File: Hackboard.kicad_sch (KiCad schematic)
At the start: 61 parts, among them J1 Conn_01x31_Socket, J2 Micro_SD_Card, J3 Conn_01x31_Socket, J5 Barrel_Jack, J6 USB_C_Receptacle_USB2.0_16P, J7 Conn_02x02_Counter_Clockwise, Q1 NMOS, Q2 NMOS, Q3 NMOS, SW1 SW_MEC_5E, U1 NCP164CSN330T1G, U2 AP63205WU, U3 STM32L476RGT6, U7 USBLC6-2SC6

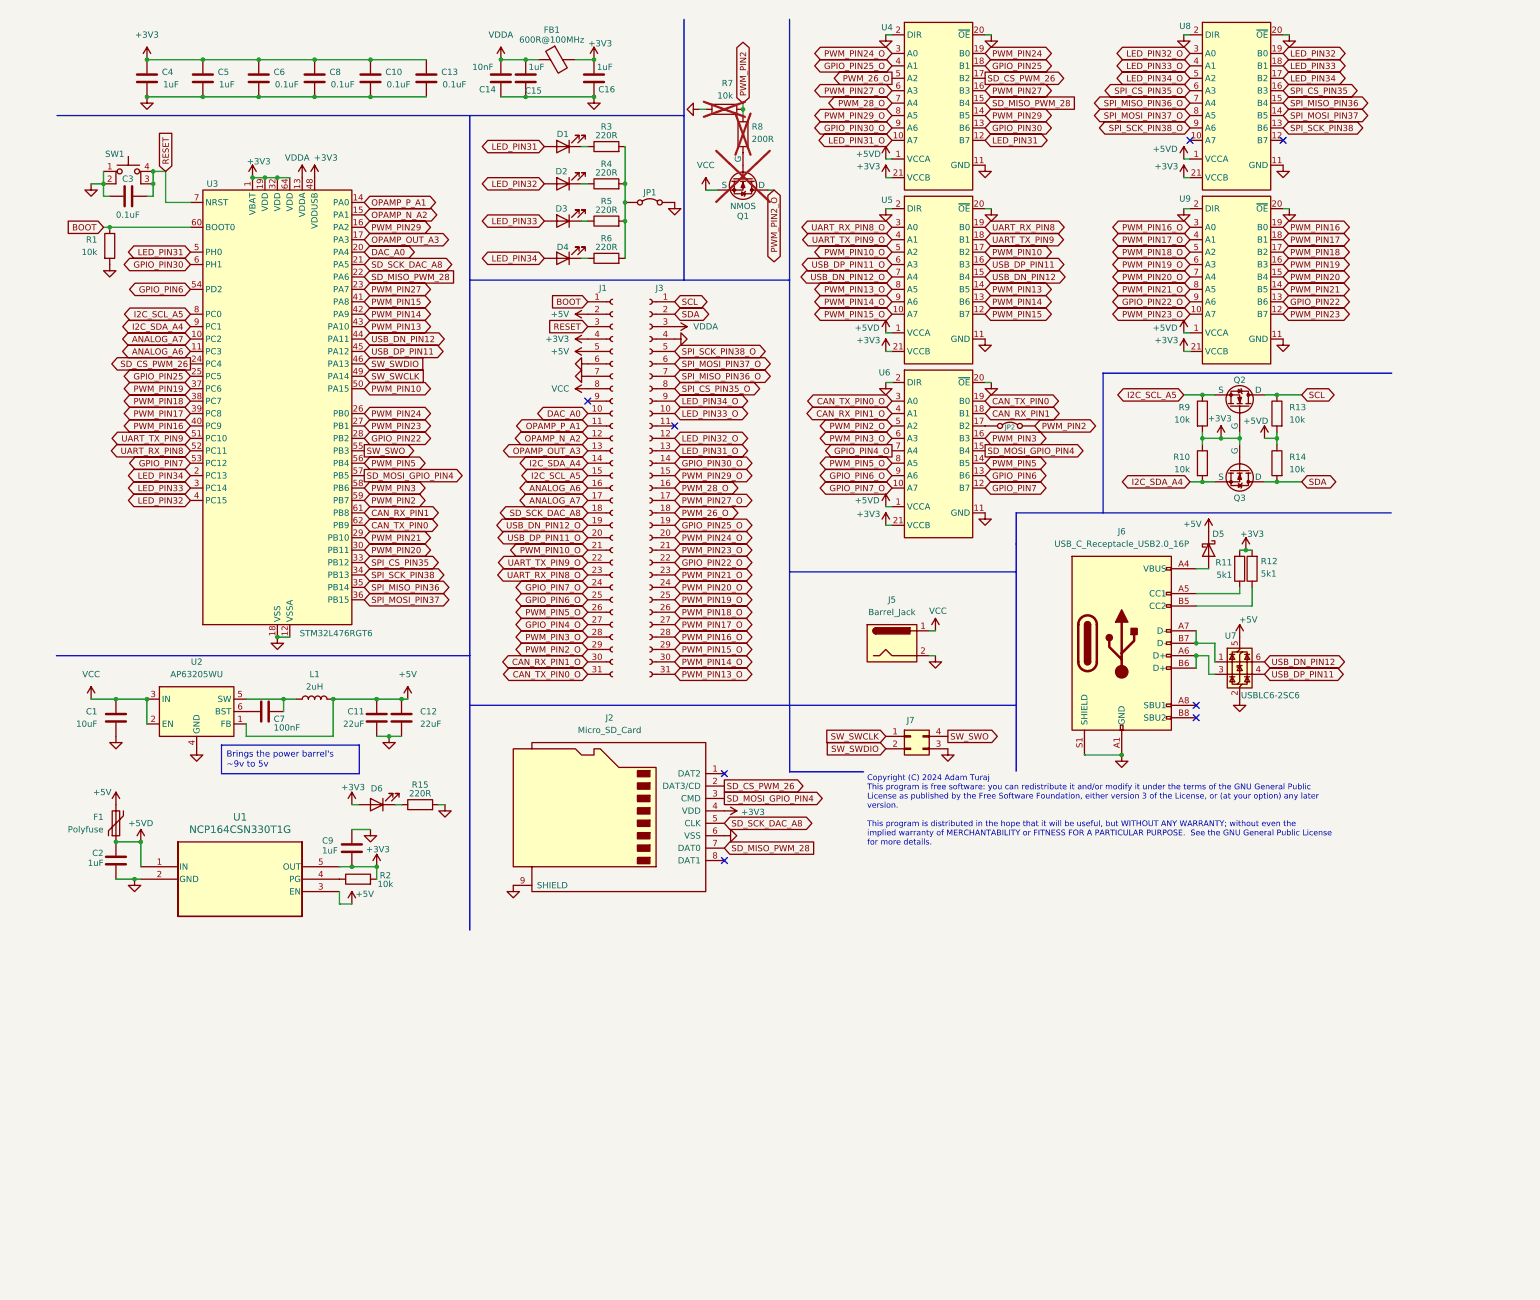
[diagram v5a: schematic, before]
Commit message: Finish footprints and place initial footprints on PCB editor
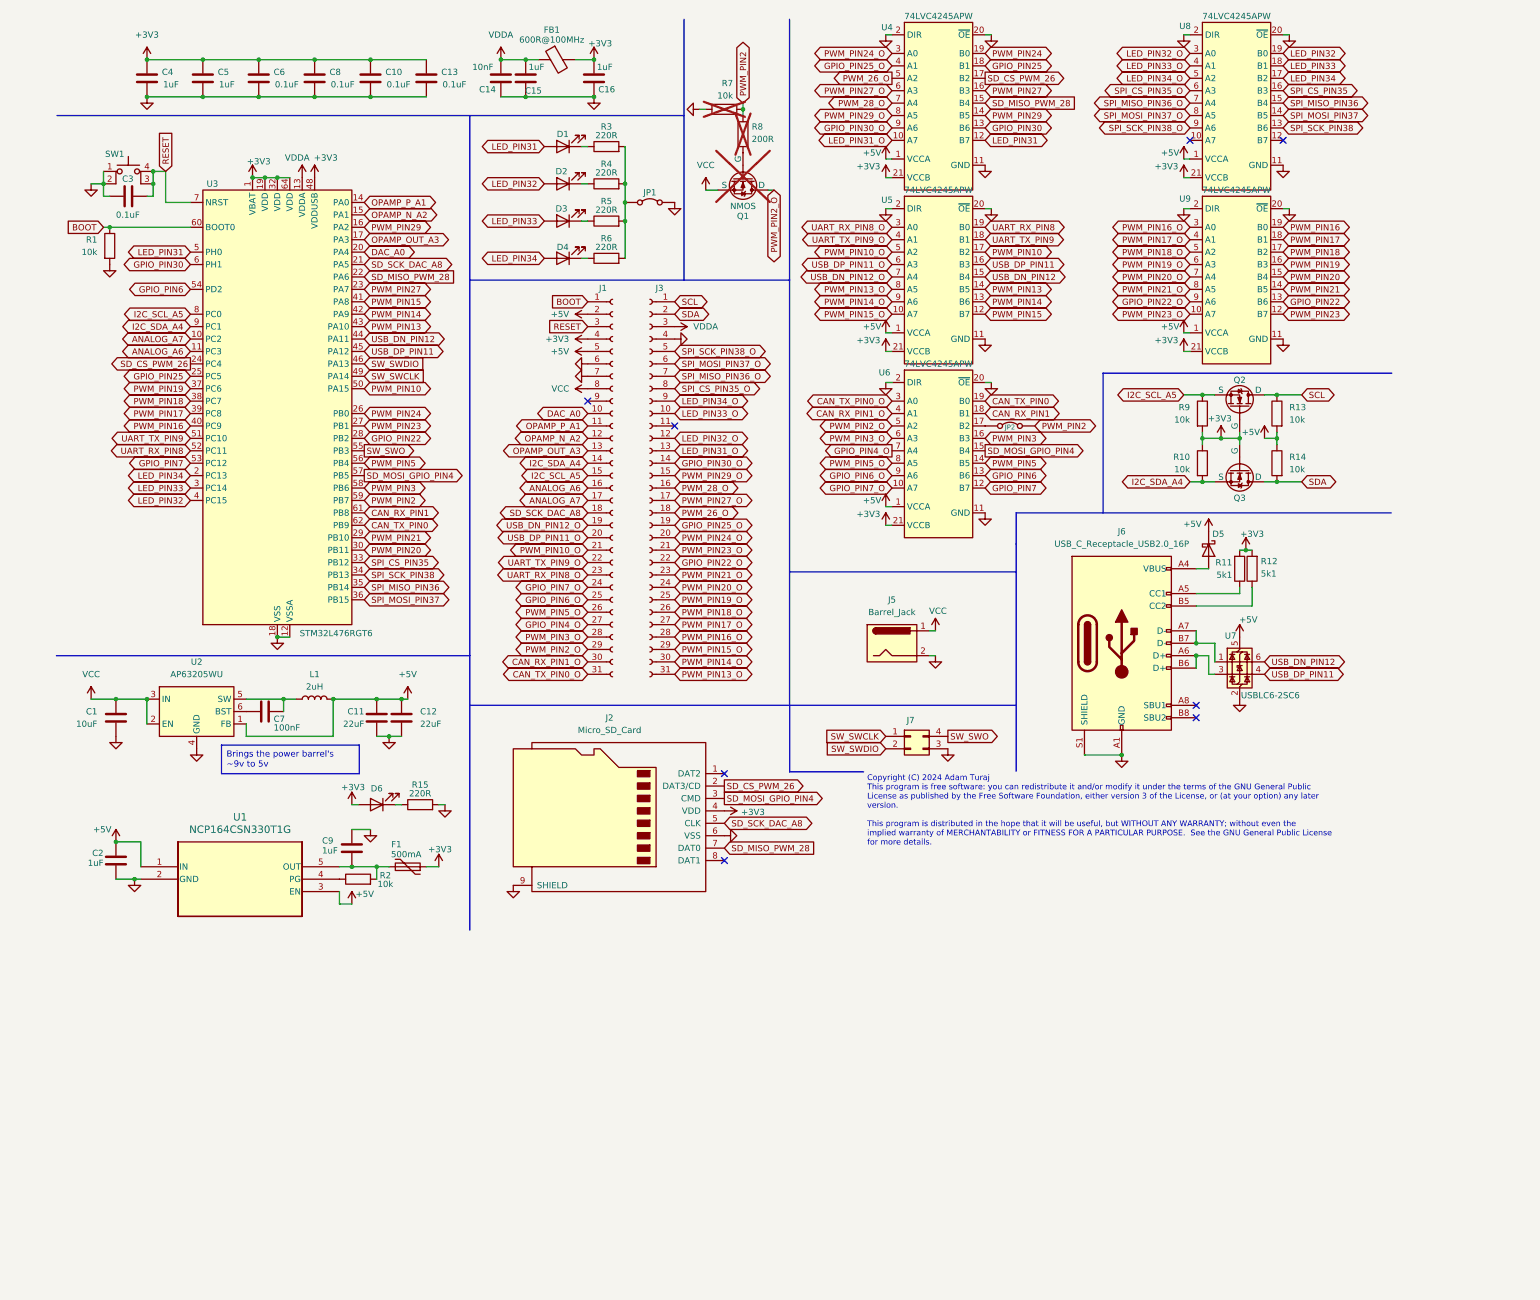
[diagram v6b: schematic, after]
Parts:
- F1: value Polyfuse -> 500mA; footprint (none) -> Fuse:Fuse_1812_4532Metric
- FB1: footprint (none) -> Inductor_SMD:L_0603_1608Metric
- J1, J3: footprint (none) -> Connector_PinHeader_2.54mm:PinHeader_1x31_P2.54mm_Vertical
- J2: footprint (none) -> Connector_Card:CONN9_MSD-1_CUD
- J5: footprint (none) -> Connector_BarrelJack:CUI_PJ-002AH
- J6: footprint (none) -> Connector_USB:USB_C_Receptacle_GCT_USB4105-xx-A_16P_TopMnt_Horizontal
- J7: footprint (none) -> Connector_PinHeader_2.54mm:PinHeader_2x02_P2.54mm_Vertical
- JP1, JP2: footprint (none) -> Jumper:SolderJumper-2_P1.3mm_Open_RoundedPad1.0x1.5mm
- Q1, Q2, Q3: footprint (none) -> Package_TO_SOT_SMD:SOT-23
- SW1: footprint (none) -> Button_Switch_SMD:SW_SPST_PTS645
- U1: footprint FP-NCP164CSN330T1G_OSI -> Package_SO:TSOP-5_1.65x3.05mm_P0.95mm
- U4, U5, U6, U8, U9: value ~ -> 74LVC4245APW; footprint (none) -> Package_SO:TSSOP-24_4.4x7.8mm_P0.65mm
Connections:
- net +3V3: now also F1.1; no longer C9.2, R2.2, U1.5 (OUT)
- net +5V: now also C2.1, R13.2, R14.1, U1.1 (IN), U4.1 (VCCA), U5.1 (VCCA), U6.1 (VCCA), U8.1 (VCCA), U9.1 (VCCA); no longer F1.2
- removed net +5VD: C2.1, F1.1, R13.2, R14.1, U1.1 (IN), U4.1 (VCCA), U5.1 (VCCA), U6.1 (VCCA), U8.1 (VCCA), U9.1 (VCCA)
- new net: C9.2, F1.2, R2.2, U1.5 (OUT)

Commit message: Make basis of out line and start placing components
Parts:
- removed J5: Barrel_Jack, Connector_BarrelJack:CUI_PJ-002AH, symbol Connector:Barrel_Jack
- removed SW1: SW_MEC_5E, Button_Switch_SMD:SW_SPST_PTS645, symbol Switch:SW_MEC_5E
- added A1: Arduino_UNO_R3, Module:Arduino_UNO_R3, symbol MCU_Module:Arduino_UNO_R3
- added H1, H2, H3, H4: MountingHole, MountingHole:MountingHole_3.2mm_M3, symbol Mechanical:MountingHole
- added J7: Barrel_Jack_Switch, Connector_BarrelJack:CUI_PJ-002AH, symbol Connector:Barrel_Jack_Switch
- added SW1: SW_DPST, Button_Switch_SMD:SW_SPST_PTS645, symbol Switch:SW_DPST_x2
- renumbered D6 to D1, D1 to D2, D2 to D3, D3 to D4, D4 to D5, D5 to D6, J7 to J5, R9 to R10, R10 to R11, R11 to R12, R12 to R13, R13 to R14, R14 to R15, R15 to R3, R3 to R4, R4 to R5, R5 to R6, R6 to R7, R7 to R8, R8 to R9
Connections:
- net CAN_RX_PIN1: now also U6.13 (B6); no longer U6.18 (B1)
- net CAN_RX_PIN1_O: now also U6.9 (A6); no longer U6.4 (A1)
- net CAN_TX_PIN0: now also U6.12 (B7); no longer U6.19 (B0)
- net CAN_TX_PIN0_O: now also U6.10 (A7); no longer U6.3 (A0)
- net GND: now also J7.2, J7.3, SW1.1 (A)
- net GPIO_PIN4_O: now also U6.6 (A3); no longer U6.7 (A4)
- net GPIO_PIN6: now also U6.18 (B1); no longer U6.13 (B6)
- net GPIO_PIN6_O: now also U6.4 (A1); no longer U6.9 (A6)
- net GPIO_PIN7: now also U6.19 (B0); no longer U6.12 (B7)
- net GPIO_PIN7_O: now also U6.3 (A0); no longer U6.10 (A7)
- net PWM_PIN10: now also U5.14 (B5); no longer U5.17 (B2)
- net PWM_PIN10_O: now also U5.8 (A5); no longer U5.5 (A2)
- net PWM_PIN13: now also U5.17 (B2); no longer U5.14 (B5)
- net PWM_PIN13_O: now also U5.5 (A2); no longer U5.8 (A5)
- net PWM_PIN14: now also U5.18 (B1); no longer U5.13 (B6)
- net PWM_PIN14_O: now also U5.4 (A1); no longer U5.9 (A6)
- net PWM_PIN15: now also U5.19 (B0); no longer U5.12 (B7)
- net PWM_PIN15_O: now also U5.3 (A0); no longer U5.10 (A7)
- net PWM_PIN2_O: now also U6.8 (A5); no longer U6.5 (A2)
- net PWM_PIN3: now also U6.15 (B4); no longer U6.16 (B3)
- net PWM_PIN3_O: now also U6.7 (A4); no longer U6.6 (A3)
- net PWM_PIN5: now also U6.17 (B2); no longer U6.14 (B5)
- net PWM_PIN5_O: now also U6.5 (A2); no longer U6.8 (A5)
- net RESET: now also SW1.2 (B)
- net SD_MOSI_GPIO_PIN4: now also U6.16 (B3); no longer U6.15 (B4)
- net UART_RX_PIN8: now also U5.12 (B7); no longer U5.19 (B0)
- net UART_RX_PIN8_O: now also U5.10 (A7); no longer U5.3 (A0)
- net UART_TX_PIN9: now also U5.13 (B6); no longer U5.18 (B1)
- net UART_TX_PIN9_O: now also U5.9 (A6); no longer U5.4 (A1)
- net USB_DN_PIN12: now also U5.16 (B3); no longer U5.15 (B4)
- net USB_DN_PIN12_O: now also U5.6 (A3); no longer U5.7 (A4)
- net USB_DP_PIN11: now also U5.15 (B4); no longer U5.16 (B3)
- net USB_DP_PIN11_O: now also U5.7 (A4); no longer U5.6 (A3)
- net VCC: now also J7.1
- net at JP2.2 (B): now also U6.14 (B5); no longer U6.17 (B2)

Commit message: Continue Laying down parts
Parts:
- removed A1: Arduino_UNO_R3, Module:Arduino_UNO_R3, symbol MCU_Module:Arduino_UNO_R3
- added C17: 0.1uF, Capacitor_SMD:C_0603_1608Metric, symbol Device:C
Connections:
- net +3V3: now also C17.1
- net GND: now also C17.2
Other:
- moved on the sheet: C10, C13, C4, C5, C6, C8
